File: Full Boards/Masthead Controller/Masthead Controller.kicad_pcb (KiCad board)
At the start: 4 copper layers, 80 x 150.1 mm, 180 parts, among them Q1 2N7002, Q2 2N7002, Q3 BSS138P,215, Q4 BSS138P,215, SW1 SW_MEC_5G, SW2 SW_MEC_5G

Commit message: Fixed the tracks running from the terminal blocks to the LDs instead of the sense resistors.
Signed-off-by: digimer <digital.mermaid@gmail.com>
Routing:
- net Net-(LD10-ISENSE): track 21.0 -> 24.4 mm
- net Net-(LD6-ISENSE): track 21.0 -> 24.3 mm
- net Net-(LD5-ISENSE): track 21.4 -> 23.9 mm
- net Net-(LD9-ISENSE): track 21.4 -> 23.8 mm
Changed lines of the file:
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@@
 	)
 	(segment
+		(start 114.6 123.5)
+		(end 125.672 123.5)
+		(width 0.4)
+		(layer "F.Cu")
+		(net "Net-(LD6-ISENSE)")
+	)
+	(segment
 		(start 127.4 123.8)
 		(end 127.4 123.5)
@@
 	)
 	(segment
-		(start 125.3 124)
-		(end 127.2 124)
+		(start 127.4 123.5)
+		(end 126.672 122.772)
 		(width 0.1524)
 		(layer "F.Cu")
@@
 	)
 	(segment
-		(start 126.672 122.772)
-		(end 126.672 122.5)
+		(start 127.1 124.1)
+		(end 127.4 123.8)
 		(width 0.1524)
 		(layer "F.Cu")
@@
 	)
 	(segment
-		(start 124.17115 124.525021)
-		(end 124.774979 124.525021)
-		(width 0.1524)
+		(start 113.4 124.7)
+		(end 114.6 123.5)
+		(width 0.4)
 		(layer "F.Cu")
 		(net "Net-(LD6-ISENSE)")
 	)
 	(segment
-		(start 127.4 123.5)
-		(end 126.672 122.772)
+		(start 124.774979 124.525021)
+		(end 125.2 124.1)
 		(width 0.1524)
 		(layer "F.Cu")
@@
 	)
 	(segment
-		(start 127.2 124)
-		(end 127.4 123.8)
+		(start 124.17115 124.525021)
+		(end 124.774979 124.525021)
 		(width 0.1524)
 		(layer "F.Cu")
@@
 	)
 	(segment
-		(start 124.774979 124.525021)
-		(end 125.3 124)
-		(width 0.1524)
+		(start 125.672 123.5)
+		(end 126.672 122.5)
+		(width 0.4)
 		(layer "F.Cu")
 		(net "Net-(LD6-ISENSE)")
 	)
 	(segment
-		(start 113.4 124.7)
-		(end 113.574979 124.525021)
-		(width 0.4)
+		(start 126.672 122.772)
+		(end 126.672 122.5)
+		(width 0.1524)
 		(layer "F.Cu")
 		(net "Net-(LD6-ISENSE)")
 	)
 	(segment
-		(start 113.574979 124.525021)
-		(end 124.17115 124.525021)
-		(width 0.4)
+		(start 125.2 124.1)
+		(end 127.1 124.1)
+		(width 0.1524)
 		(layer "F.Cu")
 		(net "Net-(LD6-ISENSE)")
@@
 	)
 	(segment
-		(start 113.4 157.700001)
-		(end 113.500001 157.700001)
-		(width 0.4)
-		(layer "F.Cu")
-		(net "Net-(LD9-ISENSE)")
-	)
-	(segment
 		(start 108.4 157.700001)
 		(end 113.4 157.700001)
@@
 	)
 	(segment
-		(start 113.500001 157.700001)
-		(end 114.625021 158.825021)
-		(width 0.4)
-		(layer "F.Cu")
-		(net "Net-(LD9-ISENSE)")
-	)
-	(segment
 		(start 127.4 157.8)
 		(end 126.672 157.072)
@@
 	)
 	(segment
-		(start 114.625021 158.825021)
-		(end 124.17115 158.825021)
+		(start 113.4 157.700001)
+		(end 113.500001 157.6)
+		(width 0.4)
+		(layer "F.Cu")
+		(net "Net-(LD9-ISENSE)")
+	)
+	(segment
+		(start 125.872 157.6)
+		(end 126.672 156.8)
 		(width 0.4)
 		(layer "F.Cu")
@@
 	)
 	(segment
+		(start 113.500001 157.6)
+		(end 125.872 157.6)
+		(width 0.4)
+		(layer "F.Cu")
+		(net "Net-(LD9-ISENSE)")
+	)
+	(segment
 		(start 124.774979 158.825021)
 		(end 125.3 158.3)
@@
 	)
 	(segment
-		(start 113.4 147.7)
-		(end 113.574979 147.525021)
-		(width 0.4)
-		(layer "F.Cu")
-		(net "Net-(LD10-ISENSE)")
-	)
-	(segment
 		(start 125.2 147.1)
 		(end 127.2 147.1)
@@
 	)
 	(segment
+		(start 114.6 146.5)
+		(end 125.672 146.5)
+		(width 0.4)
+		(layer "F.Cu")
+		(net "Net-(LD10-ISENSE)")
+	)
+	(segment
 		(start 108.4 147.7)
 		(end 113.4 147.7)
@@
 	)
 	(segment
-		(start 127.2 147.1)
-		(end 127.4 146.9)
-		(width 0.1524)
+		(start 125.672 146.5)
+		(end 126.672 145.5)
+		(width 0.4)
 		(layer "F.Cu")
 		(net "Net-(LD10-ISENSE)")
 	)
 	(segment
-		(start 113.574979 147.525021)
-		(end 124.17115 147.525021)
+		(start 113.4 147.7)
+		(end 114.6 146.5)
 		(width 0.4)
 		(layer "F.Cu")
@@
 	)
 	(segment
+		(start 127.2 147.1)
+		(end 127.4 146.9)
+		(width 0.1524)
+		(layer "F.Cu")
+		(net "Net-(LD10-ISENSE)")
+	)
+	(segment
 		(start 124.774979 147.525021)
 		(end 125.2 147.1)
@@
 	)
 	(segment
-		(start 114.099999 135.4)
-		(end 114.375021 135.675021)
+		(start 113.600001 134.5)
+		(end 125.772 134.5)
 		(width 0.4)
 		(layer "F.Cu")
@@
 	)
 	(segment
-		(start 114.375021 135.675021)
-		(end 124.17115 135.675021)
+		(start 125.772 134.5)
+		(end 126.672 133.6)
 		(width 0.4)
 		(layer "F.Cu")
@@
 	(segment
 		(start 113.4 134.700001)
-		(end 114.099999 135.4)
+		(end 113.600001 134.5)
 		(width 0.4)
 		(layer "F.Cu")

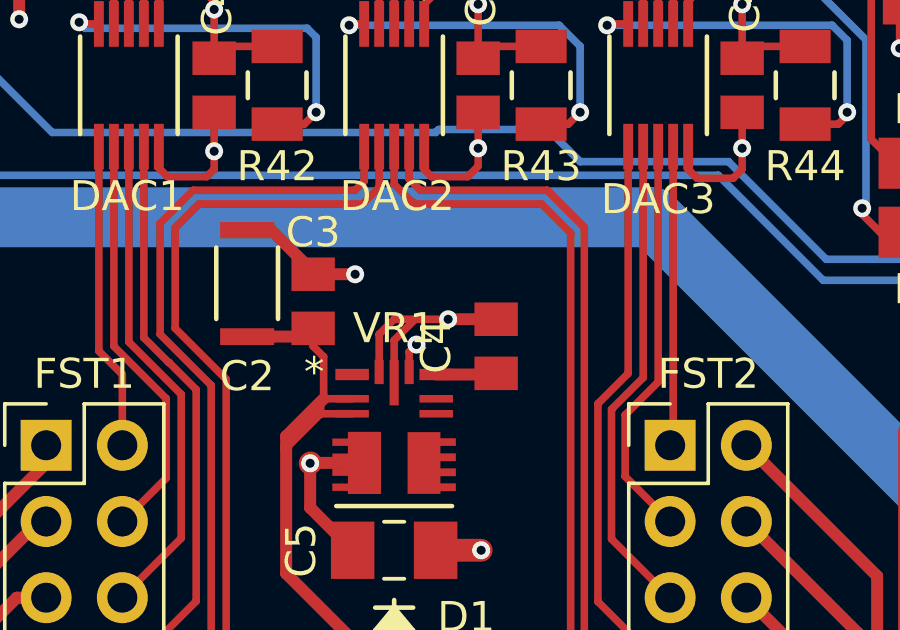
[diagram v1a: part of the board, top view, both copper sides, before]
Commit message: Implemented the update to MODE/SYNC to +3.3V.
Signed-off-by: digimer <digital.mermaid@gmail.com>
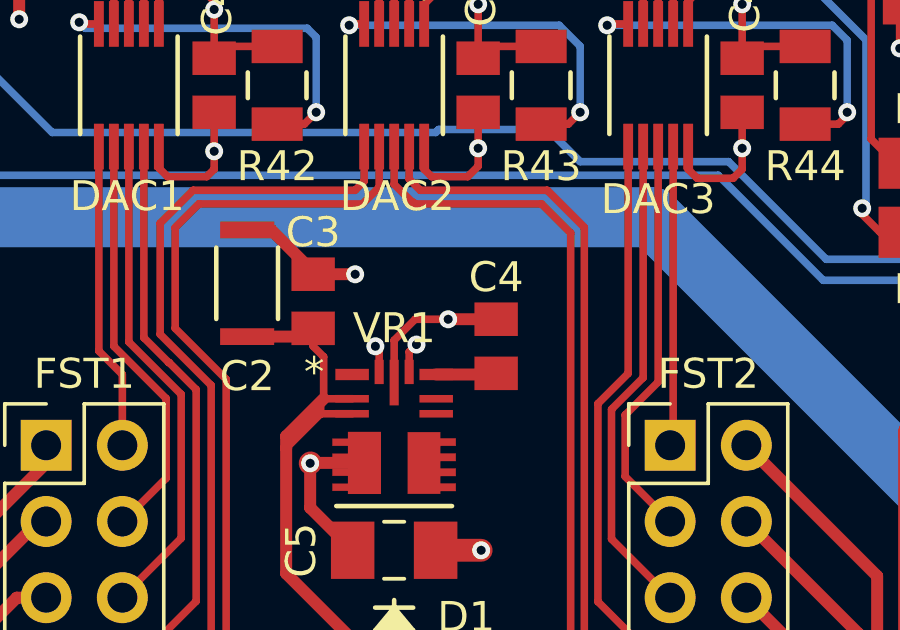
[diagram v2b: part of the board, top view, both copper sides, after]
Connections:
- VR1 pad 11: GND -> +3.3V
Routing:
- net GND: track 295.4 -> 292.7 mm
- net +3.3V: track 67.1 -> 68.0 mm, vias 14 -> 15
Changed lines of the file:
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@@
 		(tags "08051C105K4Z2A ")
 		(property "Reference" "C4"
-			(at 0 -2 90)
+			(at 2.3 0 0)
 			(unlocked yes)
 			(layer "F.SilkS")
@@
 			(size 0.3048 0.8128)
 			(layers "F.Cu" "F.Mask" "F.Paste")
-			(net "GND")
+			(net "+3.3V")
 			(pinfunction "MODE/SYNC_11")
 			(pintype "unspecified")
@@
 	)
 	(segment
-		(start 100 67.8)
-		(end 100.7 67.8)
-		(width 0.254)
-		(layer "F.Cu")
-		(net "GND")
-	)
-	(segment
 		(start 111.6 62.8)
 		(end 111.3 63.1)
@@
 	)
 	(segment
-		(start 99.5 69.554411)
-		(end 99.5 68.3)
-		(width 0.254)
-		(layer "F.Cu")
-		(net "GND")
-	)
-	(segment
 		(start 73.578 122.378)
 		(end 73.1 121.9)
@@
 	)
 	(segment
-		(start 99.5 68.3)
-		(end 100 67.8)
-		(width 0.254)
-		(layer "F.Cu")
-		(net "GND")
-	)
-	(segment
 		(start 123.224993 125.824993)
 		(end 122.8 125.4)
@@
 	)
 	(segment
+		(start 99.5 68.827)
+		(end 99.373 68.7)
+		(width 0.254)
+		(layer "F.Cu")
+		(net "+3.3V")
+	)
+	(segment
 		(start 77.3046 58.4)
 		(end 77.3046 59.6954)
@@
 	)
 	(segment
+		(start 99.5 69.554411)
+		(end 99.5 68.827)
+		(width 0.254)
+		(layer "F.Cu")
+		(net "+3.3V")
+	)
+	(segment
 		(start 69.6 50.8)
 		(end 68.7 49.9)
@@
 		(size 0.6)
 		(drill 0.3)
+		(layers "F.Cu" "B.Cu")
+		(net "+3.3V")
+	)
+	(via
+		(at 99.373 68.7)
+		(size 0.6)
+		(drill 0.3)

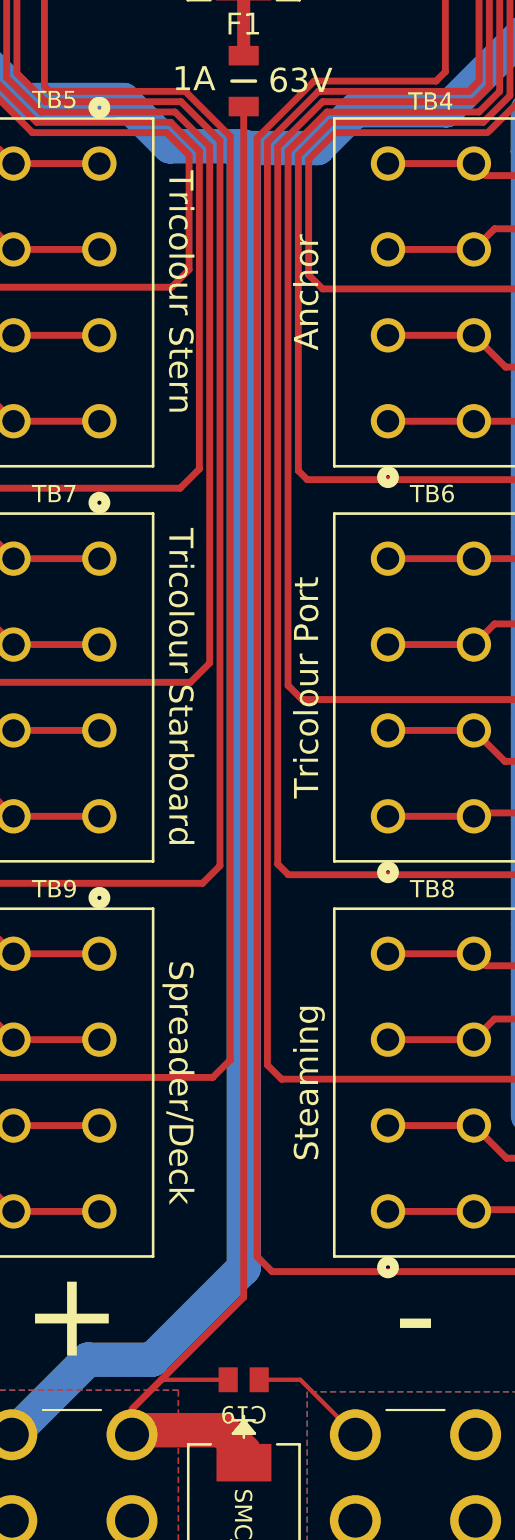
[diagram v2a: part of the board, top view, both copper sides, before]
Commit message: Added a second 0.1uF capacitor to the +24V_ISO input to help compensate for mast-length power cables.
Signed-off-by: digimer <digital.mermaid@gmail.com>
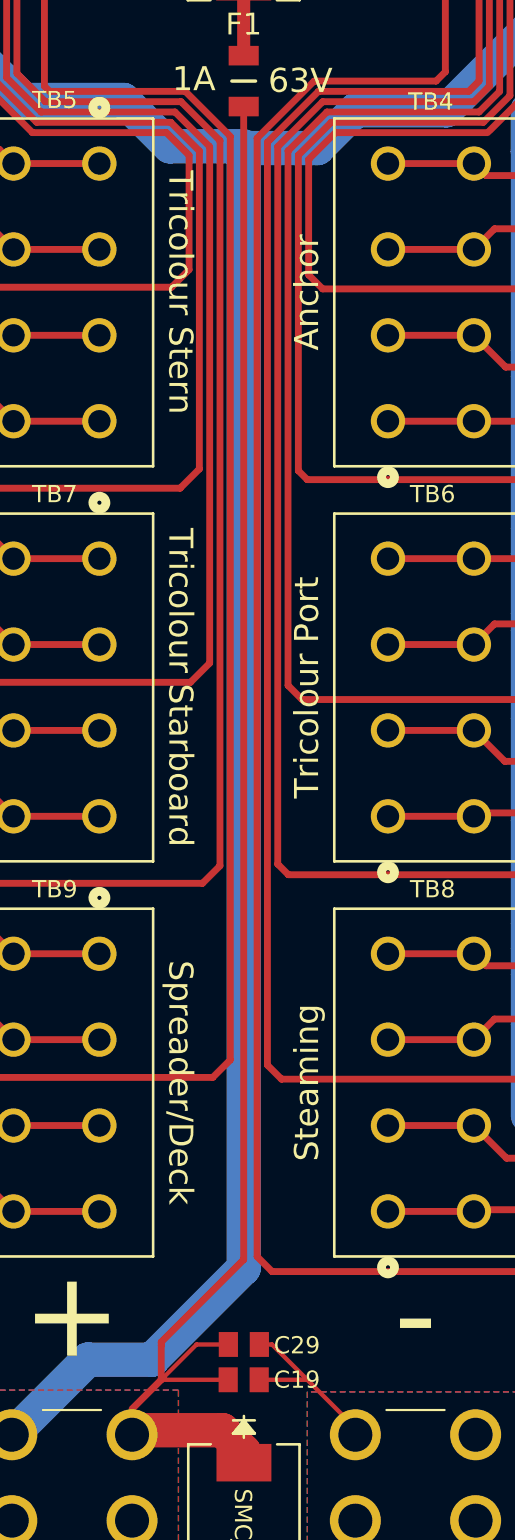
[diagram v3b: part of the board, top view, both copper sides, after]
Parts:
- added C29: 1uF, mr-stuff:Kyocera AVX 0805, F.Cu at (100.0, 165.4)
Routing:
- net +24V_ISO: track 333.4 -> 338.3 mm
- net GND: track 292.7 -> 296.6 mm

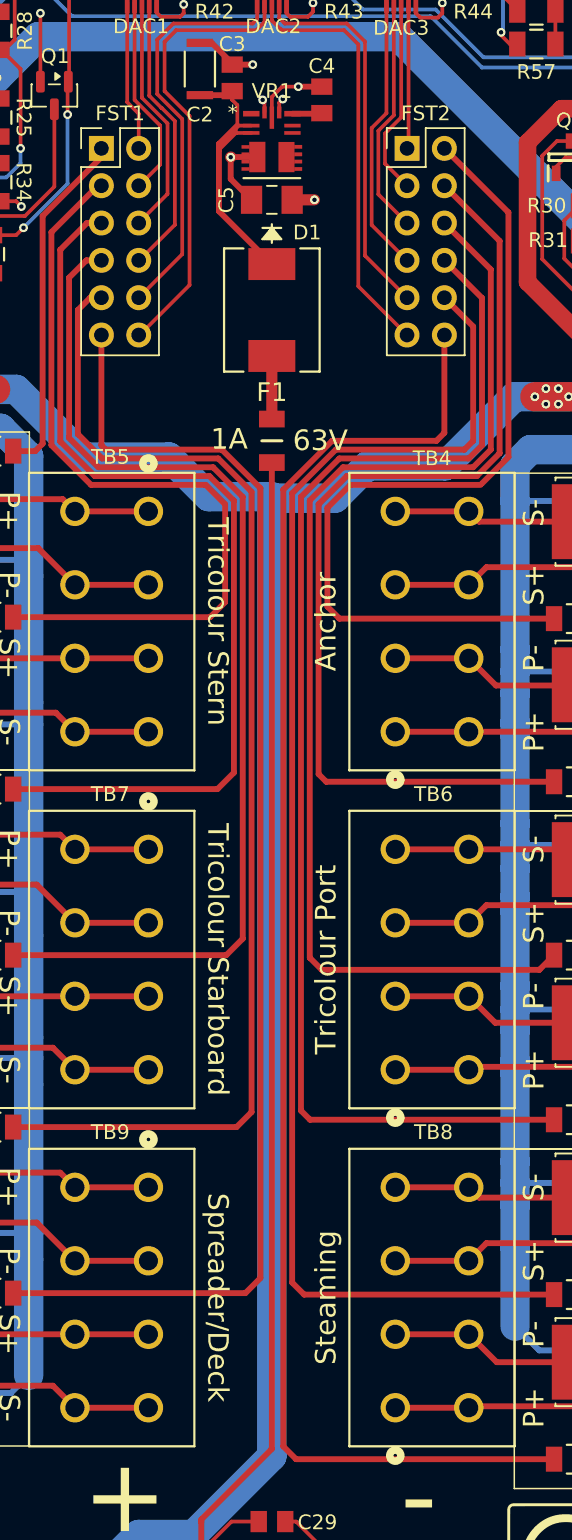
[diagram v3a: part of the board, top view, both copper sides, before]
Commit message: Updated the VOUT capacitance from 22uF to 44uF and bumped the voltage from 10V to 16V to better match the requirements of the TPSM33610S3QRDNRQ1 datasheet.
Signed-off-by: digimer <digital.mermaid@gmail.com>
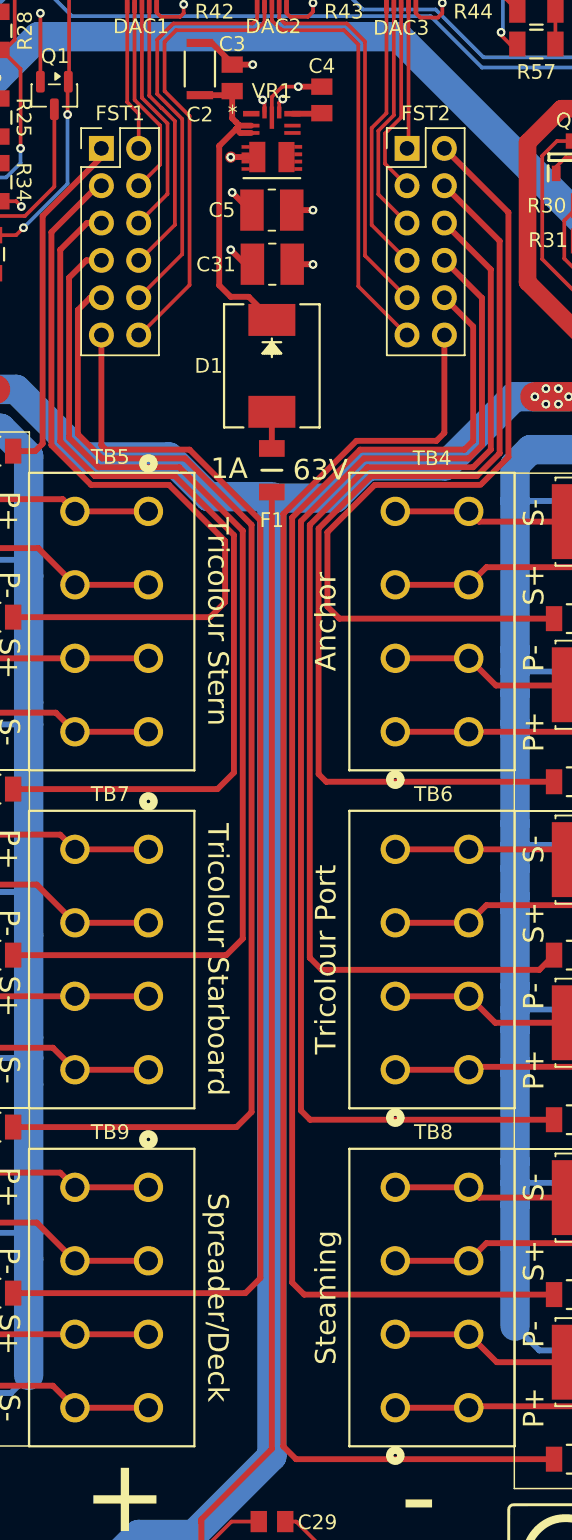
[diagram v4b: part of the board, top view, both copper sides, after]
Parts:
- added C31: 22uF, mr-stuff:Murata GCJ32ER71C, F.Cu at (100.0, 79.9)
- C5: footprint mr-stuff:Murata GCJ31CR71A -> mr-stuff:Murata GCJ32ER71C
- moved D1 3.80 mm to (100.0, 86.8)
- moved F1 2.00 mm to (100.0, 93.9)
- moved C5 0.70 mm to (100.0, 76.2)
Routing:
- net Net-(VR1-EN): track 20.0 -> 23.1 mm
- net +24V_ISO: track 338.3 -> 336.3 mm
- net Net-(D1-Pad2): track 4.29 -> 2.49 mm
- net Net-(FST1-Pin_3): track 54.0 -> 52.5 mm
- net Net-(FST1-Pin_5): track 64.1 -> 62.7 mm
- net GND: track 296.6 -> 297.9 mm, vias 186 -> 187
- net Net-(FST1-Pin_7): track 73.2 -> 71.9 mm
- net Net-(FST1-Pin_9): track 82.7 -> 81.4 mm
- net Net-(FST1-Pin_11): track 90.5 -> 89.2 mm
- net Net-(FST2-Pin_8): track 86.7 -> 85.7 mm
- net Net-(FST2-Pin_6): track 79.0 -> 78.0 mm
- net Net-(FST2-Pin_4): track 68.1 -> 67.2 mm
- net Net-(FST2-Pin_2): track 58.9 -> 57.9 mm
- net Net-(FST2-Pin_12): track 103.1 -> 102.1 mm
- net Net-(FST2-Pin_10): track 96.2 -> 95.3 mm
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
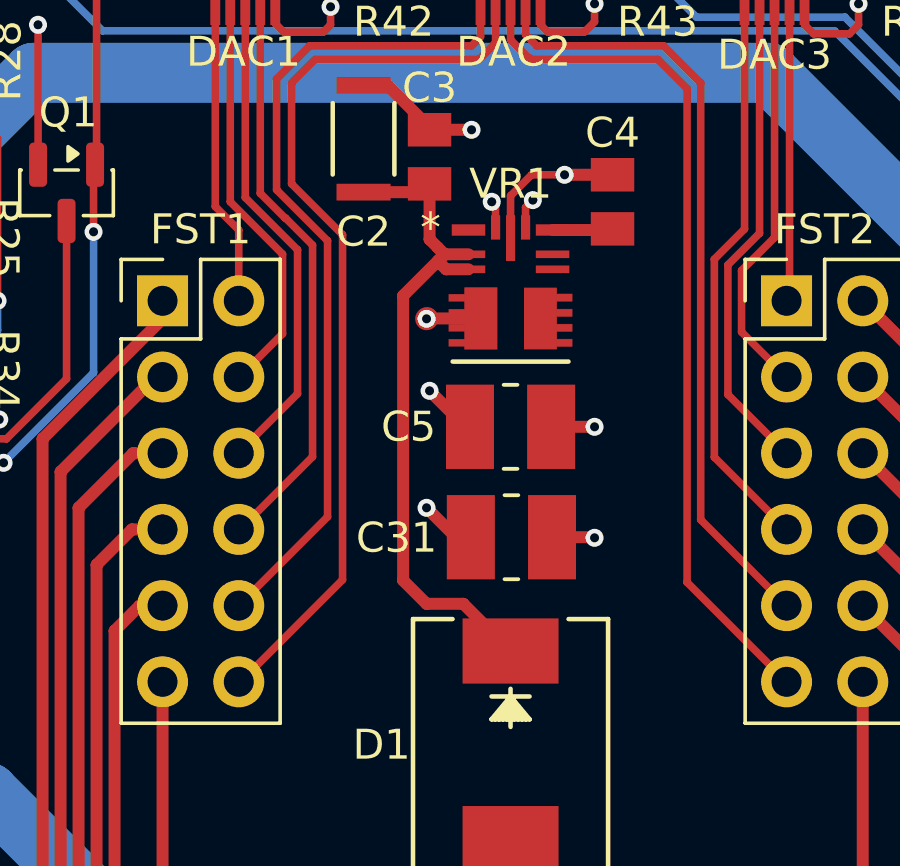
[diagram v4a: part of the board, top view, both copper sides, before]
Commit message: Added a third cap to VR1's Vout.
Signed-off-by: digimer <digital.mermaid@gmail.com>
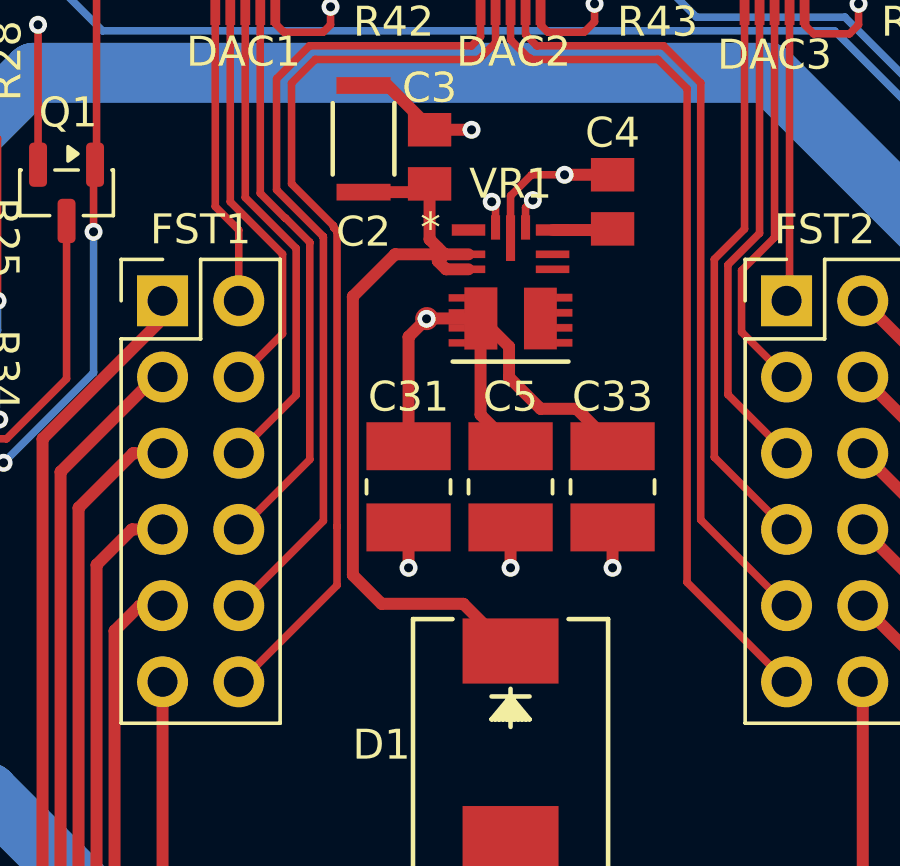
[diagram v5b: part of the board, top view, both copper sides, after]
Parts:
- added C33: 22uF, mr-stuff:Murata GCJ32ER71C, F.Cu at (103.4, 78.2)
- moved C31 3.82 mm to (96.6, 78.2), turned to -90 degrees
- moved C5 2.00 mm to (100.0, 78.2), turned to -90 degrees
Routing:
- net +3.3V: track 68.3 -> 80.5 mm, vias 17 -> 15
- net Net-(VR1-EN): track 23.1 -> 26.3 mm
- net GND: track 297.9 -> 299.1 mm, vias 187 -> 188
